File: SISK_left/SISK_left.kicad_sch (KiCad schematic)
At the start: 64 parts, among them J1 OLED_128x32, J2 Battery Socket, SW1 "Esc", SW10 "E", SW11 "R", SW12 "T", SW13 "Caps Lock", SW14 "A", SW15 "S", SW16 "D", SW17 "F", SW18 "G", SW19 "Left Shift", SW2 "1", SW20 ">", SW21 "Y", SW22 "X", SW23 "C", SW24 "V", SW25 "B", SW26 "Ctrl", SW27 "Super", SW28 "Alt", SW29 "FN", SW3 "2", SW30 "Space", SW31 SW_SPDT, SW4 "3", SW5 "4", SW6 "5", SW7 "Tab", SW8 "Q", SW9 "W", U1 Nice_Nano_V2

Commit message: changed nice nano footprint
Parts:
- U1: footprint ScottoKeebs_MCU:Arduino_Pro_Micro -> nice-nano-kicad-master:nice_nano
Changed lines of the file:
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@@
 			)
 		)
-		(property "Footprint" "ScottoKeebs_MCU:Arduino_Pro_Micro"
+		(property "Footprint" "nice-nano-kicad-master:nice_nano"
 			(at 195.58 83.82 0)
 			(effects

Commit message: added some text and alternative header for Power Switch
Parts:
- added J3: alternative ON/OFF SW(wired), Connector_PinHeader_2.54mm:PinHeader_1x02_P2.54mm_Vertical, symbol Connector_Generic:Conn_01x02
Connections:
- net at J2.1 (Pin_1), SW31.1 (A): now also J3.2 (Pin_2)
- net at SW31.2 (B), U1.24 (B+): now also J3.1 (Pin_1)
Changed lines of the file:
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@@
 	)
 	(junction
+		(at 215.9 46.99)
+		(diameter 0)
+		(color 0 0 0 0)
+	)
+	(junction
 		(at 80.01 92.71)
 		(diameter 0)
@@
 	)
 	(junction
+		(at 234.95 41.91)
+		(diameter 0)
+		(color 0 0 0 0)
+	)
+	(junction
 		(at 69.85 59.69)
 		(diameter 0)
@@
 	(wire
 		(pts
+			(xy 215.9 31.75) (xy 224.79 31.75)
+		)
+		(stroke
+			(width 0)
+			(type default)
+		)
+	)
+	(wire
+		(pts
 			(xy 80.01 102.87) (xy 80.01 106.68)
 		)
@@
 	(wire
 		(pts
+			(xy 215.9 46.99) (xy 215.9 31.75)
+		)
+		(stroke
+			(width 0)
+			(type default)
+		)
+	)
+	(wire
+		(pts
 			(xy 31.75 81.28) (xy 31.75 102.87)
 		)
@@
 	(wire
 		(pts
+			(xy 215.9 46.99) (xy 220.98 46.99)
+		)
+		(stroke
+			(width 0)
+			(type default)
+		)
+	)
+	(wire
+		(pts
 			(xy 95.25 38.1) (xy 95.25 59.69)
 		)
@@
 	(wire
 		(pts
+			(xy 227.33 31.75) (xy 234.95 31.75)
+		)
+		(stroke
+			(width 0)
+			(type default)
+		)
+	)
+	(wire
+		(pts
 			(xy 226.06 54.61) (xy 210.82 54.61)
 		)
@@
 	(wire
 		(pts
+			(xy 234.95 31.75) (xy 234.95 41.91)
+		)
+		(stroke
+			(width 0)
+			(type default)
+		)
+	)
+	(wire
+		(pts
 			(xy 95.25 102.87) (xy 95.25 106.68)
 		)
@@
 	(wire
 		(pts
-			(xy 210.82 46.99) (xy 220.98 46.99)
+			(xy 210.82 46.99) (xy 215.9 46.99)
 		)
 		(stroke
@@
 	)
 	(symbol
+		(lib_id "Connector_Generic:Conn_01x02")
+		(at 224.79 26.67 90)
+		(unit 1)
+		(exclude_from_sim no)
+		(in_bom yes)
+		(on_board yes)
+		(dnp no)
+		(fields_autoplaced yes)
+		(property "Reference" "J3"
+			(at 229.87 25.3999 90)
+			(effects
+				(font
+					(size 1.27 1.27)
+				)
+				(justify right)
+			)
+		)
+		(property "Value" "alternative ON/OFF SW(wired)"
+			(at 229.87 27.9399 90)
+			(effects
+				(font
+					(size 1.27 1.27)
+				)
+				(justify right)
+			)
+		)
+		(property "Footprint" "Connector_PinHeader_2.54mm:PinHeader_1x02_P2.54mm_Vertical"
+			(at 224.79 26.67 0)
+			(effects
+				(font
+					(size 1.27 1.27)
+				)
+				(hide yes)
+			)
+		)
+		(property "Datasheet" "~"
+			(at 224.79 26.67 0)
+			(effects
+				(font
+					(size 1.27 1.27)
+				)
+				(hide yes)
+			)
+		)
+		(property "Description" "Generic connector, single row, 01x02, script generated (kicad-library-utils/schlib/autogen/connector/)"
+			(at 224.79 26.67 0)
+			(effects
+				(font
+					(size 1.27 1.27)
+				)
+				(hide yes)
+			)
+		)
+		(pin "1"
+		)
+		(pin "2"
+		)
+		(instances
+			(project ""
+				(path "/99dcbd5e-f63f-486b-b0e7-a7e7dc92d23d"
+					(reference "J3")
+					(unit 1)
+				)
+			)
+		)
+	)
+	(symbol
 		(lib_id "Device:D")
 		(at 67.31 110.49 90)
@@
 		(on_board yes)
 		(dnp no)
-		(fields_autoplaced yes)
 		(property "Reference" "#FLG01"
 			(at 238.76 45.085 0)
@@
 		)
 		(property "Value" "PWR_FLAG"
-			(at 238.76 41.91 0)
+			(at 243.586 42.672 0)
 			(effects
 				(font

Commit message: changed file structure, added new project for 60%, changed main footprints for hotswap sockets
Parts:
- SW1, SW10, SW11, SW12, SW14, SW15, SW16, SW17, SW18, SW2, SW20, SW21, SW22, SW23, SW24, SW25, SW3, SW4, SW5, SW6, SW8, SW9: footprint ScottoKeebs_Hotswap:Hotswap_MX_Plated_1.00u -> MX_Hotswap:MX-Hotswap-1U
- SW13: footprint ScottoKeebs_Hotswap:Hotswap_MX_Plated_1.75u -> MX_Hotswap:MX-Hotswap-1.75U
- SW19, SW26, SW27, SW28, SW29: footprint ScottoKeebs_Hotswap:Hotswap_MX_Plated_1.25u -> MX_Hotswap:MX-Hotswap-1.25U
- SW30: footprint ScottoKeebs_Hotswap:Hotswap_MX_Plated_2.25u -> MX_Hotswap:MX-Hotswap-2.25U
- SW7: footprint ScottoKeebs_Hotswap:Hotswap_MX_Plated_1.50u -> MX_Hotswap:MX-Hotswap-1.5U
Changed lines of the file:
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@@
 			)
 		)
-		(property "Footprint" "ScottoKeebs_Hotswap:Hotswap_MX_Plated_1.00u"
+		(property "Footprint" "MX_Hotswap:MX-Hotswap-1U"
 			(at 87.63 54.61 0)
 			(effects
@@
 			)
 		)
-		(property "Footprint" "ScottoKeebs_Hotswap:Hotswap_MX_Plated_1.25u"
+		(property "Footprint" "MX_Hotswap:MX-Hotswap-1.25U"
 			(at 36.83 119.38 0)
 			(effects
@@
 			)
 		)
-		(property "Footprint" "ScottoKeebs_Hotswap:Hotswap_MX_Plated_1.00u"
+		(property "Footprint" "MX_Hotswap:MX-Hotswap-1U"
 			(at 87.63 76.2 0)
 			(effects
@@
 			)
 		)
-		(property "Footprint" "ScottoKeebs_Hotswap:Hotswap_MX_Plated_1.00u"
+		(property "Footprint" "MX_Hotswap:MX-Hotswap-1U"
 			(at 49.53 33.02 0)
 			(effects
@@
 			)
 		)
-		(property "Footprint" "ScottoKeebs_Hotswap:Hotswap_MX_Plated_1.00u"
+		(property "Footprint" "MX_Hotswap:MX-Hotswap-1U"
 			(at 49.53 76.2 0)
 			(effects
@@
 			)
 		)
-		(property "Footprint" "ScottoKeebs_Hotswap:Hotswap_MX_Plated_1.00u"
+		(property "Footprint" "MX_Hotswap:MX-Hotswap-1U"
 			(at 100.33 97.79 0)
 			(effects
@@
 			)
 		)
-		(property "Footprint" "ScottoKeebs_Hotswap:Hotswap_MX_Plated_1.00u"
+		(property "Footprint" "MX_Hotswap:MX-Hotswap-1U"
 			(at 62.23 97.79 0)
 			(effects
@@
 			)
 		)
-		(property "Footprint" "ScottoKeebs_Hotswap:Hotswap_MX_Plated_1.00u"
+		(property "Footprint" "MX_Hotswap:MX-Hotswap-1U"
 			(at 100.33 54.61 0)
 			(effects
@@
 			)
 		)
-		(property "Footprint" "ScottoKeebs_Hotswap:Hotswap_MX_Plated_1.00u"
+		(property "Footprint" "MX_Hotswap:MX-Hotswap-1U"
 			(at 113.03 97.79 0)
 			(effects
@@
 			)
 		)
-		(property "Footprint" "ScottoKeebs_Hotswap:Hotswap_MX_Plated_1.00u"
+		(property "Footprint" "MX_Hotswap:MX-Hotswap-1U"
 			(at 100.33 76.2 0)
 			(effects
@@
 			)
 		)
-		(property "Footprint" "ScottoKeebs_Hotswap:Hotswap_MX_Plated_1.00u"
+		(property "Footprint" "MX_Hotswap:MX-Hotswap-1U"
 			(at 49.53 97.79 0)
 			(effects
@@
 			)
 		)
-		(property "Footprint" "ScottoKeebs_Hotswap:Hotswap_MX_Plated_1.00u"
+		(property "Footprint" "MX_Hotswap:MX-Hotswap-1U"
 			(at 74.93 54.61 0)
 			(effects
@@
 			)
 		)
-		(property "Footprint" "ScottoKeebs_Hotswap:Hotswap_MX_Plated_1.00u"
+		(property "Footprint" "MX_Hotswap:MX-Hotswap-1U"
 			(at 49.53 54.61 0)
 			(effects
@@
 			)
 		)
-		(property "Footprint" "ScottoKeebs_Hotswap:Hotswap_MX_Plated_1.00u"
+		(property "Footprint" "MX_Hotswap:MX-Hotswap-1U"
 			(at 74.93 33.02 0)
 			(effects
@@
 			)
 		)
-		(property "Footprint" "ScottoKeebs_Hotswap:Hotswap_MX_Plated_1.00u"
+		(property "Footprint" "MX_Hotswap:MX-Hotswap-1U"
 			(at 87.63 97.79 0)
 			(effects
@@
 			)
 		)
-		(property "Footprint" "ScottoKeebs_Hotswap:Hotswap_MX_Plated_1.00u"
+		(property "Footprint" "MX_Hotswap:MX-Hotswap-1U"
 			(at 36.83 33.02 0)
 			(effects
@@
 			)
 		)
-		(property "Footprint" "ScottoKeebs_Hotswap:Hotswap_MX_Plated_1.00u"
+		(property "Footprint" "MX_Hotswap:MX-Hotswap-1U"
 			(at 87.63 33.02 0)
 			(effects
@@
 			)
 		)
-		(property "Footprint" "ScottoKeebs_Hotswap:Hotswap_MX_Plated_1.75u"
+		(property "Footprint" "MX_Hotswap:MX-Hotswap-1.75U"
 			(at 36.83 76.2 0)
 			(effects
@@
 			)
 		)
-		(property "Footprint" "ScottoKeebs_Hotswap:Hotswap_MX_Plated_1.25u"
+		(property "Footprint" "MX_Hotswap:MX-Hotswap-1.25U"
 			(at 74.93 119.38 0)
 			(effects
@@
 			)
 		)
-		(property "Footprint" "ScottoKeebs_Hotswap:Hotswap_MX_Plated_1.00u"
+		(property "Footprint" "MX_Hotswap:MX-Hotswap-1U"
 			(at 62.23 76.2 0)
 			(effects
@@
 			)
 		)
-		(property "Footprint" "ScottoKeebs_Hotswap:Hotswap_MX_Plated_1.00u"
+		(property "Footprint" "MX_Hotswap:MX-Hotswap-1U"
 			(at 62.23 54.61 0)
 			(effects
@@
 			)
 		)
-		(property "Footprint" "ScottoKeebs_Hotswap:Hotswap_MX_Plated_1.00u"
+		(property "Footprint" "MX_Hotswap:MX-Hotswap-1U"
 			(at 74.93 76.2 0)
 			(effects
@@
 			)
 		)
-		(property "Footprint" "ScottoKeebs_Hotswap:Hotswap_MX_Plated_1.00u"
+		(property "Footprint" "MX_Hotswap:MX-Hotswap-1U"
 			(at 100.33 33.02 0)
 			(effects
@@
 			)
 		)
-		(property "Footprint" "ScottoKeebs_Hotswap:Hotswap_MX_Plated_1.00u"
+		(property "Footprint" "MX_Hotswap:MX-Hotswap-1U"
 			(at 62.23 33.02 0)
 			(effects
@@
 			)
 		)
-		(property "Footprint" "ScottoKeebs_Hotswap:Hotswap_MX_Plated_2.25u"
+		(property "Footprint" "MX_Hotswap:MX-Hotswap-2.25U"
 			(at 87.63 119.38 0)
 			(effects
@@
 			)
 		)
-		(property "Footprint" "ScottoKeebs_Hotswap:Hotswap_MX_Plated_1.00u"
+		(property "Footprint" "MX_Hotswap:MX-Hotswap-1U"
 			(at 74.93 97.79 0)
 			(effects
@@
 			)
 		)
-		(property "Footprint" "ScottoKeebs_Hotswap:Hotswap_MX_Plated_1.25u"
+		(property "Footprint" "MX_Hotswap:MX-Hotswap-1.25U"
 			(at 36.83 97.79 0)
 			(effects
@@
 			)
 		)
-		(property "Footprint" "ScottoKeebs_Hotswap:Hotswap_MX_Plated_1.25u"
+		(property "Footprint" "MX_Hotswap:MX-Hotswap-1.25U"
 			(at 49.53 119.38 0)
 			(effects
@@
 			)
 		)
-		(property "Footprint" "ScottoKeebs_Hotswap:Hotswap_MX_Plated_1.25u"
+		(property "Footprint" "MX_Hotswap:MX-Hotswap-1.25U"
 			(at 62.23 119.38 0)
 			(effects
@@
 			)
 		)
-		(property "Footprint" "ScottoKeebs_Hotswap:Hotswap_MX_Plated_1.50u"
+		(property "Footprint" "MX_Hotswap:MX-Hotswap-1.5U"
 			(at 36.83 54.61 0)
 			(effects

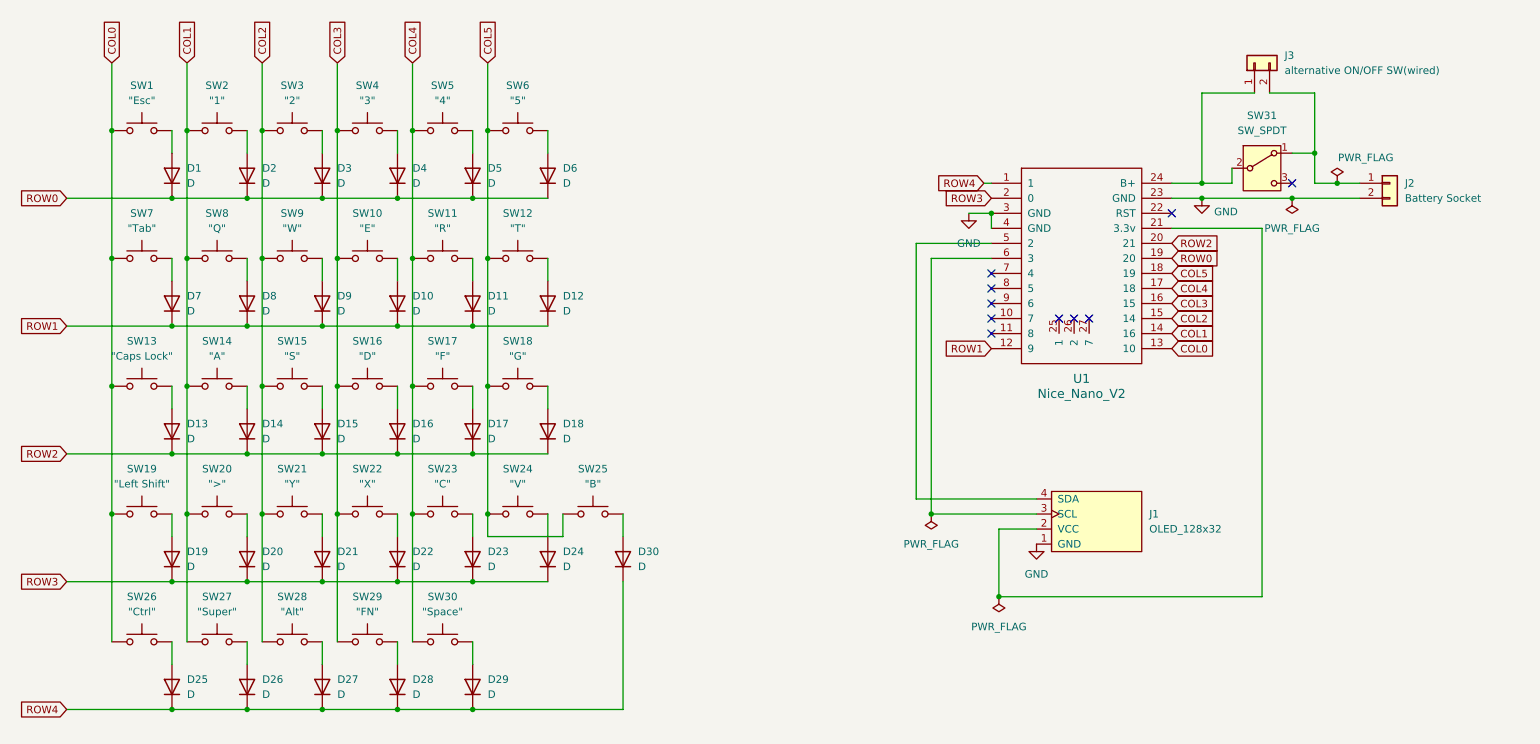
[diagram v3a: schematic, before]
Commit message: fixed schematics, added optional pullup resistors
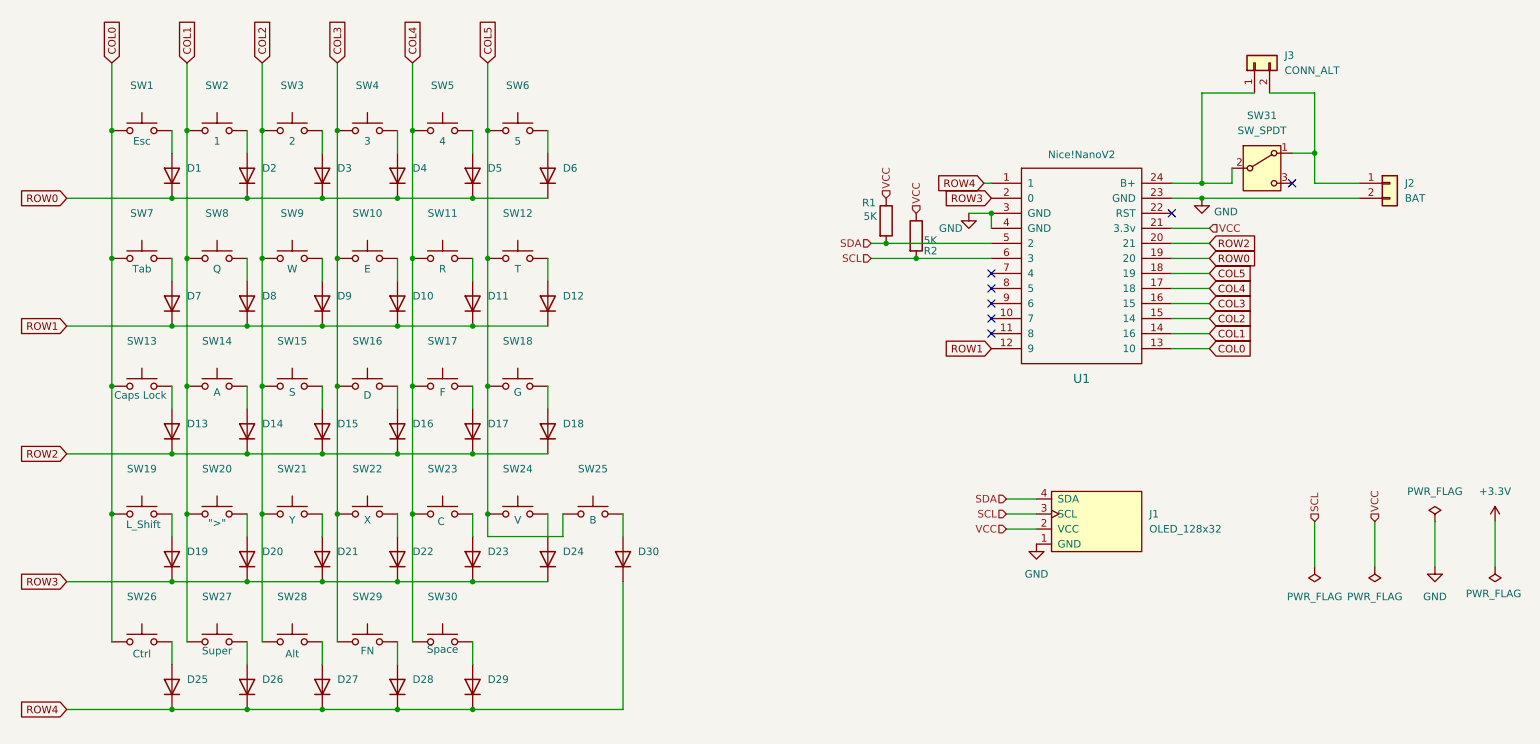
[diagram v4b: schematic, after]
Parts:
- added R1, R2: 5K, Resistor_SMD:R_1206_3216Metric_Pad1.30x1.75mm_HandSolder, symbol Device:R
- D1, D10, D11, D12, D13, D14, D15, D16, D17, D18, D19, D2, D20, D21, D22, D23, D24, D25, D26, D27, D28, D29, D3, D30, D4, D5, D6, D7, D8, D9: value D -> 1n4148
- J1: Label (none) -> OLED_128x32
- J2: value Battery Socket -> BAT; Label (none) -> Battery conn
- J3: value alternative ON/OFF SW(wired) -> CONN_ALT; Label (none) -> alternative ON/OFF SW(wired)
- SW1: value "Esc" -> SW_push; Label (none) -> Esc
- SW10: value "E" -> SW_push; Label (none) -> E
- SW11: value "R" -> SW_push; Label (none) -> R
- SW12: value "T" -> SW_push; Label (none) -> T
- SW13: value "Caps Lock" -> SW_push; Label (none) -> Caps Lock
- SW14: value "A" -> SW_push; Label (none) -> A
- SW15: value "S" -> SW_push; Label (none) -> S
- SW16: value "D" -> SW_push; Label (none) -> D
- SW17: value "F" -> SW_push; Label (none) -> F
- SW18: value "G" -> SW_push; Label (none) -> G
- SW19: value "Left Shift" -> SW_push; Label (none) -> L_Shift
- SW2: value "1" -> SW_push; Label (none) -> 1
- SW20: value ">" -> SW_push; Label (none) -> ">"
- SW21: value "Y" -> SW_push; Label (none) -> Y
- SW22: value "X" -> SW_push; Label (none) -> X
- SW23: value "C" -> SW_push; Label (none) -> C
- SW24: value "V" -> SW_push; Label (none) -> V
- SW25: value "B" -> SW_push; Label (none) -> B
- SW26: value "Ctrl" -> SW_push; Label (none) -> Ctrl
- SW27: value "Super" -> SW_push; Label (none) -> Super
- SW28: value "Alt" -> SW_push; Label (none) -> Alt
- SW29: value "FN" -> SW_push; Label (none) -> FN
- SW3: value "2" -> SW_push; Label (none) -> 2
- SW30: value "Space" -> SW_push; Label (none) -> Space
- SW4: value "3" -> SW_push; Label (none) -> 3
- SW5: value "4" -> SW_push; Label (none) -> 4
- SW6: value "5" -> SW_push; Label (none) -> 5
- SW7: value "Tab" -> SW_push; Label (none) -> Tab
- SW8: value "Q" -> SW_push; Label (none) -> Q
- SW9: value "W" -> SW_push; Label (none) -> W
- U1: Label (none) -> Nice!NanoV2
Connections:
- net VCC: now reaches J1.2 (VCC), U1.21 (3.3v)
- net VCC: now also R1.1, R2.1
- net SCL: now reaches J1.3 (SCL), U1.6 (3)
- net SCL: now also R2.2
- net SDA: now reaches J1.4 (SDA), U1.5 (2)
- net SDA: now also R1.2
- no-connect marks 10 -> 7

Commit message: fixed most of issues, updated 60% version
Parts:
- D1, D10, D11, D12, D13, D14, D15, D16, D17, D18, D19, D2, D20, D21, D22, D23, D24, D25, D26, D27, D28, D29, D3, D30, D4, D5, D6, D7, D8, D9: MPN (none) -> 1N4148W
- J1: Label OLED_128x32 -> OLED 128x32 i2C; MPN (none) -> OLED 128x32 i2C
- J2: Label Battery conn -> Battery connector; MPN (none) -> S2B-PH-K-S(LF)(SN)
- J3: MPN (none) -> not known yet
- R1, R2: value 5K -> 2K2; MPN (none) -> RC1206JR-072K2L
- SW1, SW10, SW11, SW12, SW13, SW14, SW15, SW16, SW17, SW18, SW19, SW2, SW20, SW21, SW22, SW23, SW24, SW25, SW26, SW27, SW28, SW29, SW3, SW30, SW4, SW5, SW6, SW7, SW8, SW9: MPN (none) -> CPG151101S11
- SW31: Label (none) -> POWER ON/OFF SW (onboard); MPN (none) -> MSK12C01
- U1: MPN (none) -> nice!nano v2 or compatible
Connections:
- net VCC is gone; now on net +3.3V: J1.2 (VCC), R1.1, R2.1, U1.21 (3.3v)
- net +BATT: now reaches J2.1 (Pin_1), J3.2 (Pin_2), SW31.1 (A)
- net +VDC: now reaches J3.1 (Pin_1), SW31.2 (B), U1.24 (B+)
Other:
- moved on the sheet: J3, R1, R2

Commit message: improved the whole mounting hole situation
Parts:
- added H1, H2, H3, H4: M3, MountingHole:MountingHole_3.2mm_M3_ISO7380_Pad_TopBottom, symbol Mechanical:MountingHole
- added H5: M2, MountingHole:MountingHole_2.2mm_M2_ISO7380_Pad_TopOnly, symbol Mechanical:MountingHole
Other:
- note added: "Mounting Holes:"
